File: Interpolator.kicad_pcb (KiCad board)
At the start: 4 copper layers, 78 x 46 mm, 78 parts, among them J1 DA15_Receptacle_MountingHoles, J2 DA15_Receptacle_MountingHoles, J3 Conn_01x12, J4 Conn_01x12, SW1 SW_Push, U1 UA9638C, U2 UA9638C, U3 ICTW8, U5 24AA02-OT, U6 MCP1754S-3302xMB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

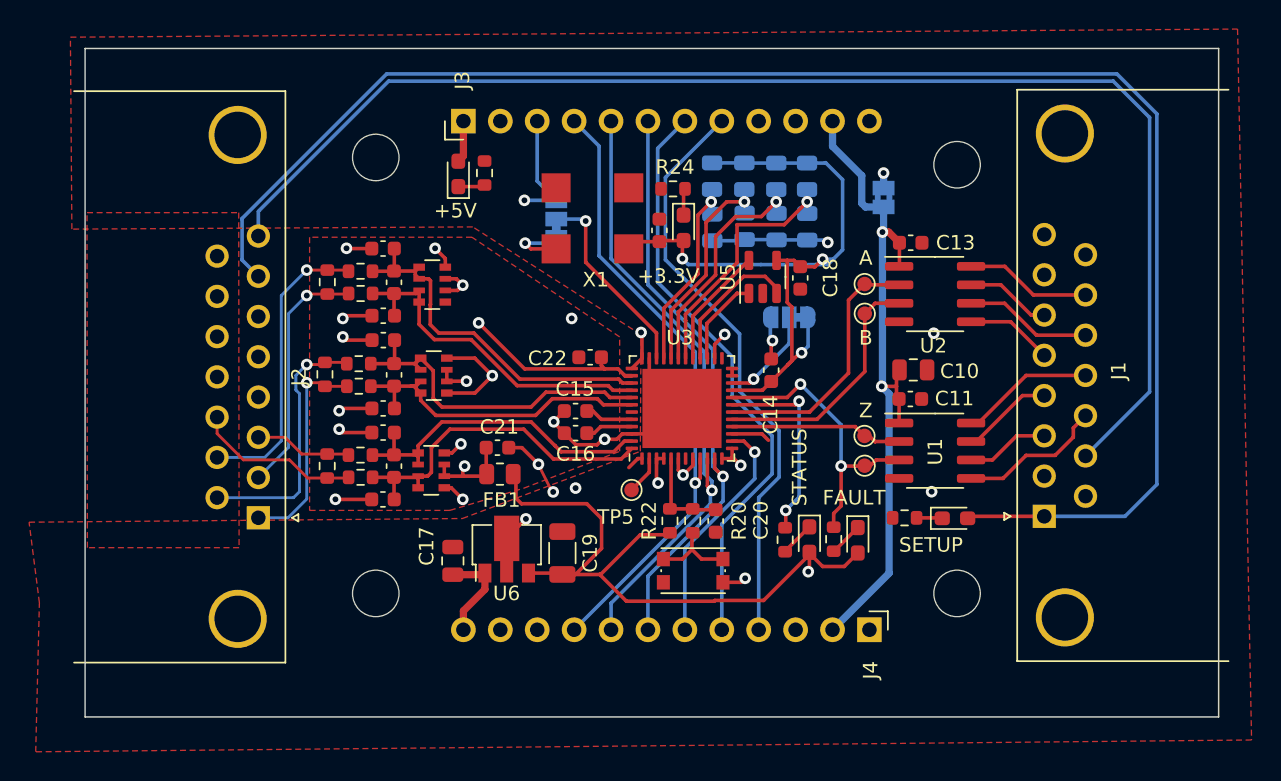
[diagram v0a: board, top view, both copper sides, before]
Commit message: Update a few footprints, remove the 5v rail power LED, move all of the LED resistors to one 20K network
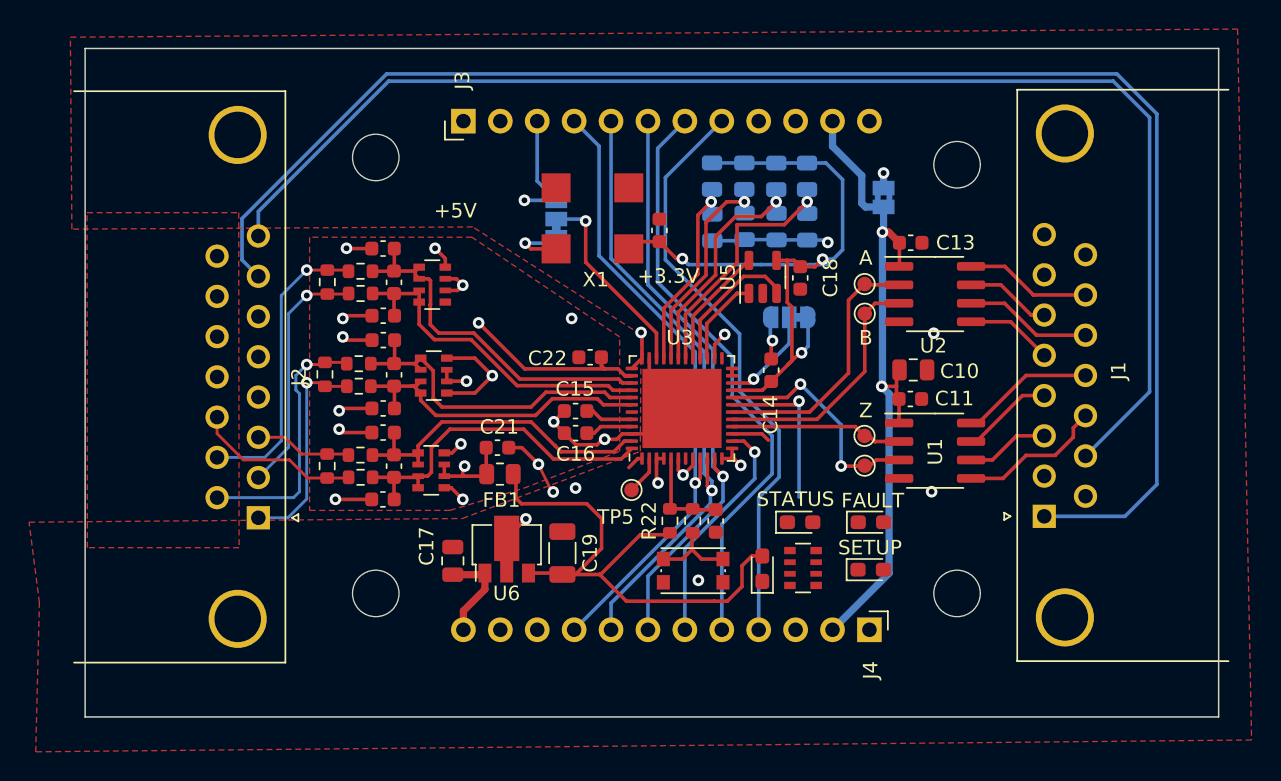
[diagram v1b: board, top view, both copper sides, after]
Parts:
- removed D4: LED, encoder-interpolator:LED_0603_1608Metric_Pad1.05x0.95mm_HandSolder
- removed R18, R19, R21, R23, R24: 20K, encoder-interpolator:R_0603_1608Metric
- added RN4: R20K, encoder-interpolator:R_Array_Convex_4x0603, F.Cu at (173.4, 69.8)
- moved D5 24.1 mm to (170.6, 69.8), turned to 90 degrees
- moved D3 6.79 mm to (178.1, 69.9)
- moved D1 4.40 mm to (178.1, 66.6), turned to 0 degrees
- moved D2 4.16 mm to (173.2, 66.6), turned to 0 degrees
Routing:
- net +3.3V: track 114.8 -> 96.1 mm, vias 4 -> 3
- net SETUP: track 112.1 -> 106.8 mm
- net FAULT: track 20.5 -> 16.1 mm
- net +5V: track 122.8 -> 119.9 mm
- net STATUS: track 13.8 -> 11.3 mm, vias 2 -> 1
- net Net-(D1-K): track 2.40 -> 0.00 mm
- net Net-(D2-K): track 2.33 -> 0.00 mm
- net Net-(D4-K): track 1.85 -> 0.00 mm
- net Net-(D5-K): track 1.85 -> 0.00 mm
- net Net-(D3-K): track 1.78 -> 0.00 mm
- net GND: track 33.8 -> 32.1 mm
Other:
- board text added: "mds - rev 1 - 1/18/25"
- board text removed: "mds - rev 0 - 12/1/24"
